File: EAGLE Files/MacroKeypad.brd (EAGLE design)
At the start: 61 x 62.2 mm, 8 parts

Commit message: Clean up old files
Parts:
- removed S2: (no value), switch:255SB
- removed U$6: CHERRY-MX, cherrymx:CHERRY-MX
- added S1: MOMENTARY-SWITCH-SPST-PTH-6.0MM, SparkFun-Switches:TACTILE_SWITCH_PTH_6.0MM
- added U$7: CHERRY-MX-LED, cherrymx:CHERRY-MX-LED
- U$1, U$2, U$3, U$4, U$5: value CHERRY-MX -> CHERRY-MX-LED; device cherrymx:CHERRY-MX -> cherrymx:CHERRY-MX-LED
- moved U$4 39.8 mm to (82.5, 59.7)
- moved U$1 17.8 mm to (47.0, 41.9)
- moved U$2 17.8 mm to (64.8, 41.9)
- moved U$3 17.8 mm to (64.8, 59.7)
- moved U$5 17.8 mm to (82.5, 41.9)
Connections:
- removed net VCC: B1.21
- new net LED+: B1.20, B1.21, U$1.LED+, U$2.LED+, U$3.LED+, U$4.LED+, U$5.LED+, U$7.LED+
- net GND: now also S1.1, U$1.LED-, U$2.LED-, U$3.LED-, U$4.LED-, U$5.LED-, U$7.LED-, U$7.SW2; no longer S2.1, U$6.SW2
- net RESET: now also S1.3; no longer S2.2
- net SW1: now also U$7.SW1; no longer U$1.SW1
- net SW2: now also U$3.SW1; no longer U$2.SW1
- net SW3: now also U$4.SW1; no longer U$3.SW1
- net SW4: now also U$1.SW1; no longer U$4.SW1
- net SW5: now also U$2.SW1; no longer U$5.SW1
- net SW6: now also U$5.SW1; no longer U$6.SW1
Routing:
- net LED+: track 0.00 -> 121.8 mm, vias 0 -> 1
- net GND: track 136.9 -> 177.2 mm
- net RESET: track 46.2 -> 44.2 mm, vias 1 -> 0
- net SW6: track 44.8 -> 45.8 mm
- net SW4: vias 2 -> 1
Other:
- board text added: "Rev 1 - L/B"
- board text removed: "Rev 1"

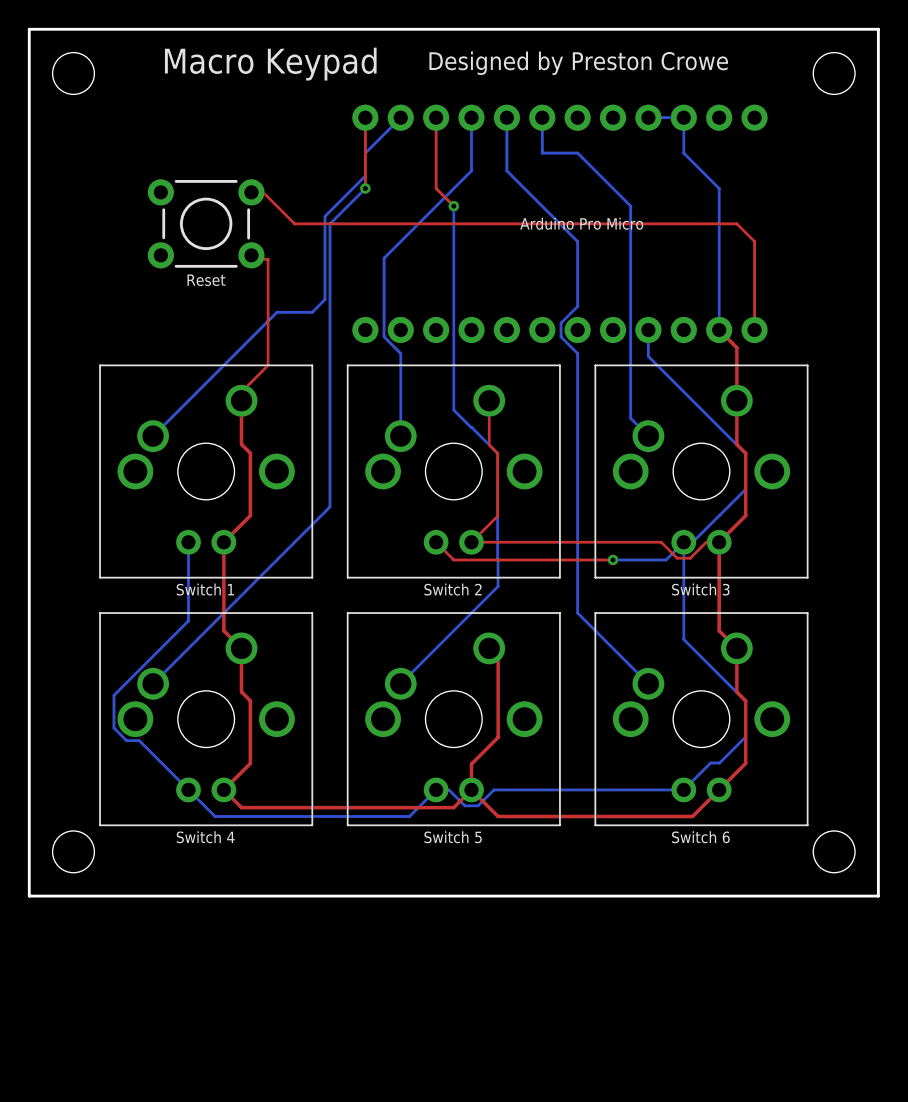
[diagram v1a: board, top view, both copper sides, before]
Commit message: Brand new PCB started
Started redesigning PCB and added BOM
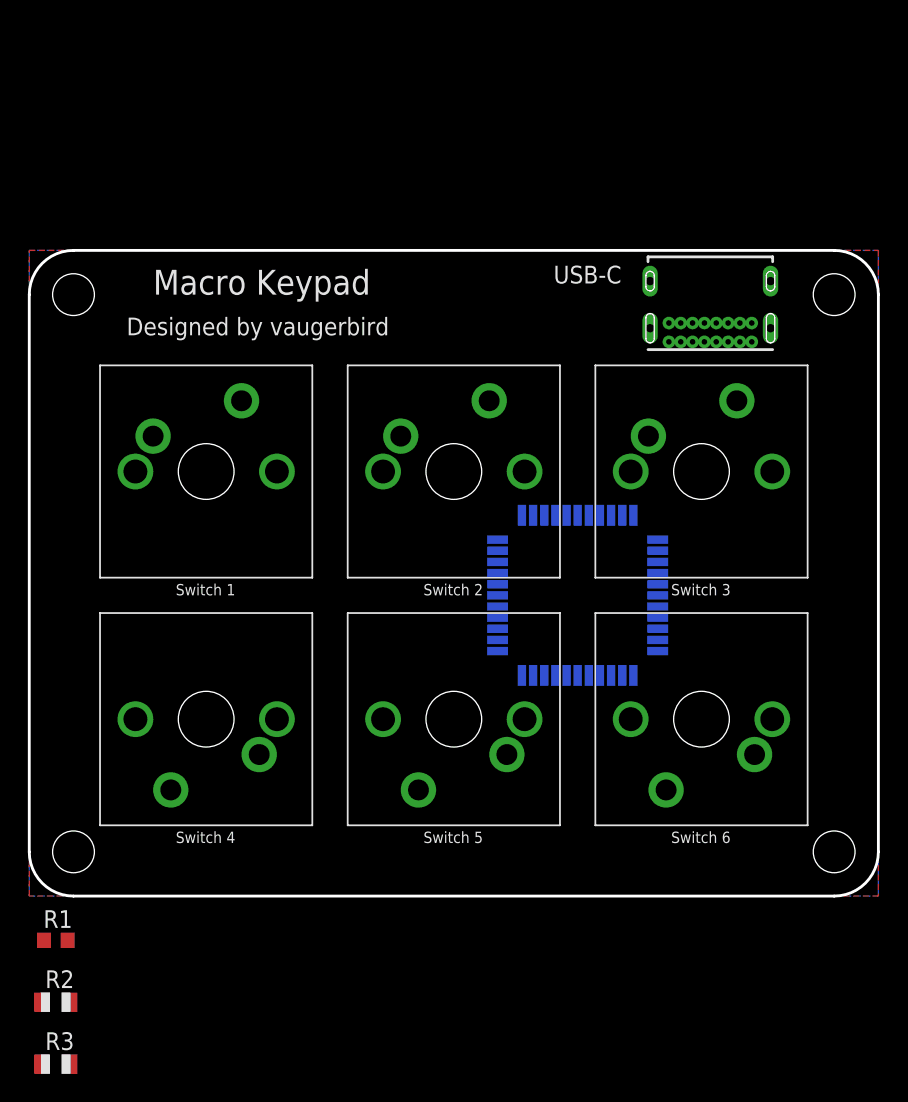
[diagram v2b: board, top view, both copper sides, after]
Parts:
- removed B1: SPARKFUN_PRO_MICRO, SparkFun-Boards:SPARKFUN_PRO_MICRO
- removed S1: MOMENTARY-SWITCH-SPST-PTH-6.0MM, SparkFun-Switches:TACTILE_SWITCH_PTH_6.0MM
- removed U$7: CHERRY-MX-LED, cherrymx:CHERRY-MX-LED
- added IC1: ATMEGA32U4-AUR, SamacSys_Parts:QFP80P1200X1200X120-44N
- added R1: (no value), adafruit:R0603
- added R2, R3: (no value), adafruit:R0805
- added U$6: CHERRY-MX, cherrymx:CHERRY-MX
- added USB-C: USB4085-GF-A_REVA, USB4085-GF-A_REVA:GCT_USB4085-GF-A_REVA
- U$1, U$2, U$3, U$4, U$5: value CHERRY-MX-LED -> CHERRY-MX; device cherrymx:CHERRY-MX-LED -> cherrymx:CHERRY-MX
- moved U$2 17.8 mm to (82.5, 41.9), turned to 180 degrees
- moved U$4 17.8 mm to (64.8, 59.7)
- moved U$5 17.8 mm to (82.5, 59.7)
- moved U$1 17.8 mm to (64.8, 41.9), turned to 180 degrees
- moved U$3 17.8 mm to (47.0, 59.7)
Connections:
- removed net LED+: B1.20, B1.21, U$1.LED+, U$2.LED+, U$3.LED+, U$4.LED+, U$5.LED+, U$7.LED+
- removed net RESET: B1.24, S1.3
- new net N$1: R1.1, USB-C.A5, USB-C.B5
- new net N$2: IC1.2, USB-C.A4, USB-C.A9, USB-C.B4, USB-C.B9
- new net N$3: R3.1, USB-C.A6, USB-C.B6
- new net N$4: R2.1, USB-C.A7, USB-C.B7
- new net N$5: IC1.3, R2.2
- new net N$6: IC1.4, R3.2
- net GND: now also IC1.15, IC1.24, IC1.35, IC1.43, IC1.5, R1.2, U$6.SW2, USB-C.A1, USB-C.A12, USB-C.B1, USB-C.B12, USB-C.P1, USB-C.P2, USB-C.P3, USB-C.P4; no longer B1.23, B1.3, B1.4, S1.1, U$1.LED-, U$2.LED-, U$3.LED-, U$4.LED-, U$5.LED-, U$7.LED-, U$7.SW2
- net SW1: now also U$6.SW1; no longer B1.11, U$7.SW1
- net SW2: no longer B1.9
- net SW3: no longer B1.7
- net SW4: no longer B1.12
- net SW5: no longer B1.10
- net SW6: no longer B1.8
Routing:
- net GND: track 177.2 -> 0.00 mm
- net LED+: track 121.8 -> 0.00 mm, vias 1 -> 0
- net SW4: track 47.0 -> 0.00 mm, vias 1 -> 0
- net SW6: track 45.8 -> 0.00 mm
- net SW5: track 45.4 -> 0.00 mm, vias 1 -> 0
- net RESET: track 44.2 -> 0.00 mm
- net SW1: track 31.7 -> 0.00 mm
- net SW3: track 27.5 -> 0.00 mm
- net SW2: track 26.0 -> 0.00 mm
- added copper zone on layer 1, net GND
- added copper zone on layer 16, net GND
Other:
- board size 61 x 62.2 mm -> 61 x 46.4 mm
- board text added: "Designed by vaugerbird"
- board text added: "Rev 2"
- board text added: "https://github.com/vaugerbird/Macro-Keypad"
- board text removed: "Arduino Pro Micro"
- board text removed: "Designed by Preston Crowe"
- board text removed: "Reset"
- board text removed: "Rev 1 - L/B"
- board text removed: "github.com/PrestonCrowe/Macro-Keypad"

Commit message: Update more files
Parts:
- removed IC1: ATMEGA32U4-AUR, SamacSys_Parts:QFP80P1200X1200X120-44N
- added C1: 1uF, adafruit:C0805
- added IC2: ATMEGA32U4-MU, SamacSys_Parts:QFN50P700X700X100-45N
- R1: value (none) -> 5.1k
- R2, R3: value (none) -> 22Ω
- moved R3 66.1 mm to (74.3, 71.1), flipped to the bottom
- moved R2 61.0 mm to (74.3, 69.2), flipped to the bottom
- moved R1 56.4 mm to (74.8, 67.2), flipped to the bottom
- moved USB-C 0.64 mm to (82.5, 73.0)
- turned SW4 to 0 degrees
- turned SW5 to 0 degrees
- turned SW6 to 0 degrees
- renumbered U$1 to SW5, U$2 to SW6, U$3 to SW1, U$4 to SW2, U$5 to SW3, U$6 to SW4
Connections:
- net N$1 renamed CC
- removed net SW1: SW4.SW1
- removed net SW2: SW1.SW1
- removed net SW3: SW2.SW1
- removed net SW4: SW5.SW1
- removed net SW5: SW6.SW1
- removed net SW6: SW3.SW1
- new net D+: R2.1, USB-C.A6, USB-C.B6
- new net D+RES: IC2.4, R2.2
- new net D-: R3.1, USB-C.A7, USB-C.B7
- new net D-RES: IC2.3, R3.2
- new net N$1: IC2.19, SW1.SW1
- new net UCAP: C1.1, IC2.6
- new net VCC: IC2.14, IC2.24, IC2.44
- new net VIN: IC2.2, USB-C.A4, USB-C.A9, USB-C.B4, USB-C.B9
- net GND: now also C1.2, IC2.15, IC2.23, IC2.35, IC2.43, IC2.5; no longer IC1.15, IC1.24, IC1.35, IC1.43, IC1.5
- net N$2: now also IC2.20, SW2.SW1; no longer IC1.2, USB-C.A4, USB-C.A9, USB-C.B4, USB-C.B9
- net N$3: now also IC2.21, SW3.SW1; no longer R3.1, USB-C.A6, USB-C.B6
- net N$4: now also IC2.25, SW4.SW1; no longer R2.1, USB-C.A7, USB-C.B7
- net N$5: now also IC2.22, SW5.SW1; no longer IC1.3, R2.2
- net N$6: now also IC2.26, SW6.SW1; no longer IC1.4, R3.2
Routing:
- net VIN: track 0.00 -> 28.9 mm
- net D+RES: track 0.00 -> 12.8 mm
- net D-RES: track 0.00 -> 12.2 mm
- net D-: track 0.00 -> 11.2 mm
- net D+: track 0.00 -> 10.6 mm
- net CC: track 0.00 -> 9.21 mm
- net UCAP: track 0.00 -> 4.21 mm

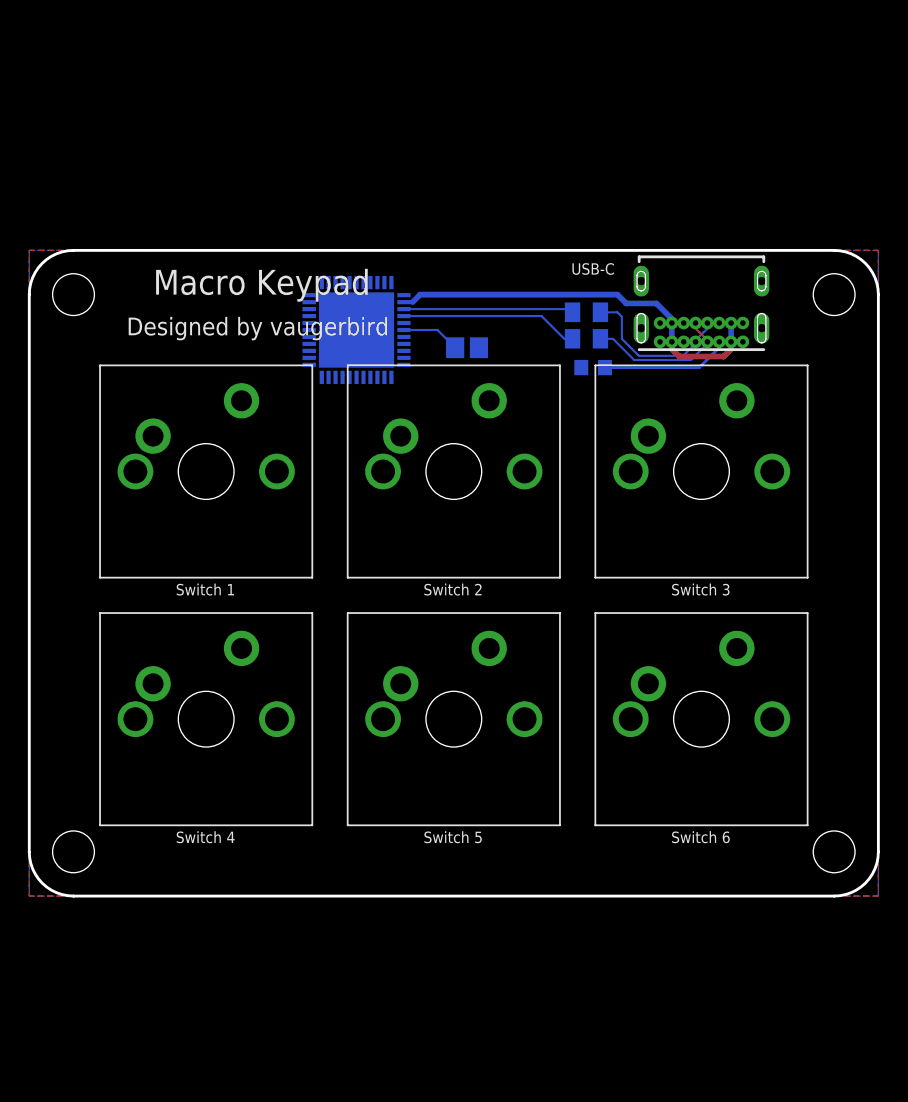
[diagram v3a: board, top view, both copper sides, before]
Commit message: (Almost) Finished with the redo
Pretty much done, just need to fix USB-C port footprint and make code for the new board
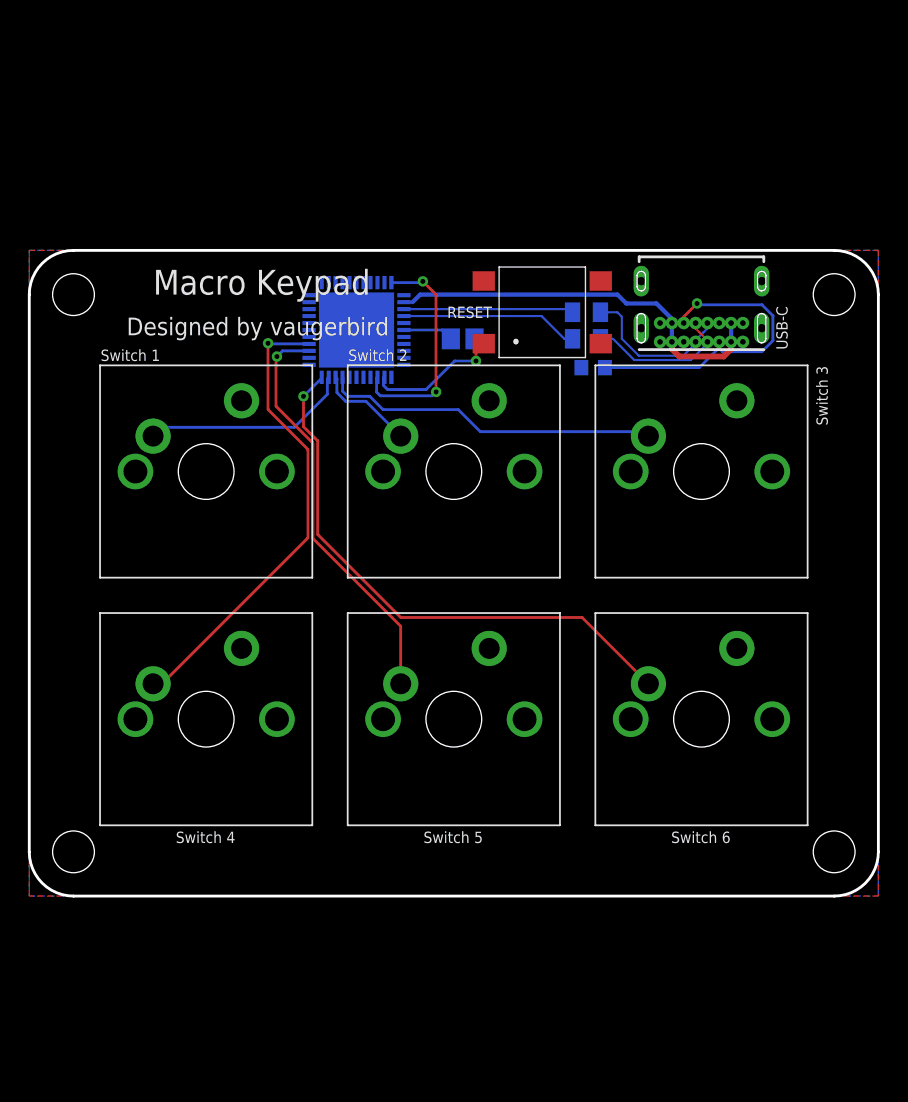
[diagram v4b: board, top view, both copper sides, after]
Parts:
- added RESET: LL3303F065QG, SamacSys_Parts:LL3303F065QG
- moved C1 0.71 mm to (65.4, 69.2)
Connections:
- net N$2 renamed SW2
- removed net N$1: IC2.19, SW1.SW1
- removed net N$3: IC2.21, SW3.SW1
- removed net N$4: IC2.25, SW4.SW1
- removed net N$5: IC2.22, SW5.SW1
- removed net N$6: IC2.26, SW6.SW1
- new net RESET: IC2.13, RESET.1
- new net SW1: IC2.21, SW1.SW1
- new net SW3: IC2.19, SW3.SW1
- new net SW4: IC2.26, SW4.SW1
- new net SW5: IC2.25, SW5.SW1
- new net SW6: IC2.22, SW6.SW1
- net GND: now also RESET.2
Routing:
- net SW6: track 0.00 -> 40.4 mm, vias 0 -> 1
- net SW4: track 0.00 -> 33.6 mm, vias 0 -> 1
- net SW5: track 0.00 -> 29.8 mm, vias 0 -> 1
- net SW3: track 0.00 -> 24.3 mm
- net VCC: track 0.00 -> 16.2 mm, vias 0 -> 2
- net SW1: track 0.00 -> 15.0 mm
- net CC: track 9.21 -> 23.0 mm, vias 0 -> 1
- net RESET: track 0.00 -> 9.69 mm, vias 0 -> 1
- net SW2: track 0.00 -> 7.01 mm
- net UCAP: track 4.21 -> 3.63 mm
